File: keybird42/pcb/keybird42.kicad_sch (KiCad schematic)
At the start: 183 parts, among them SW1 SW_MX, SW10 SW_MX, SW11 SW_MX, SW12 SW_MX, SW13 SW_MX, SW14 SW_MX, SW15 SW_MX, SW16 SW_MX, SW17 SW_MX, SW18 SW_MX, SW19 SW_MX, SW2 SW_MX, SW20 SW_MX, SW21 SW_MX, SW22 SW_MX, SW23 SW_MX, SW24 SW_MX, SW25 SW_MX, SW26 SW_MX, SW27 SW_MX, SW28 SW_MX, SW29 SW_MX, SW3 SW_MX, SW30 SW_MX, SW31 SW_MX, SW32 SW_MX, SW33 SW_MX, SW34 SW_MX, SW35 SW_MX, SW36 SW_MX, SW37 SW_MX, SW38 SW_MX, SW39 SW_MX, SW4 SW_MX, SW40 SW_MX, SW41 SW_MX, SW42 SW_MX, SW43 SW_MX, SW44 SW_MX, SW45 SW_MX, SW46 SW_MX, SW47 SW_MX, SW48 SW_MX, SW49 SW_MX, SW5 SW_MX, SW50 SW_MX, SW51 SW_MX, SW52 SW_MX, SW53 SW_MX, SW54 SW_MX, SW55 SW_MX, SW56 SW_MX, SW57 SW_MX, SW58 SW_MX, SW59 SW_MX, SW6 SW_MX, SW60 SW_MX, SW61 SW_MX, SW62 SW_MX, SW63 SW_MX, SW64 SW_MX, SW65 SW_MX, SW66 SW_MX, SW67 SW_MX, SW68 SW_MX, SW69 SW_MX, SW7 SW_MX, SW70 SW_MX, SW71 SW_MX, SW72 SW_MX, SW73 SW_MX, SW74 SW_MX, SW75 SW_MX, SW76 SW_MX, SW77 SW_MX, SW78 SW_MX, SW79 SW_MX, SW8 SW_MX, SW80 SW_MX, SW81 SW_MX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

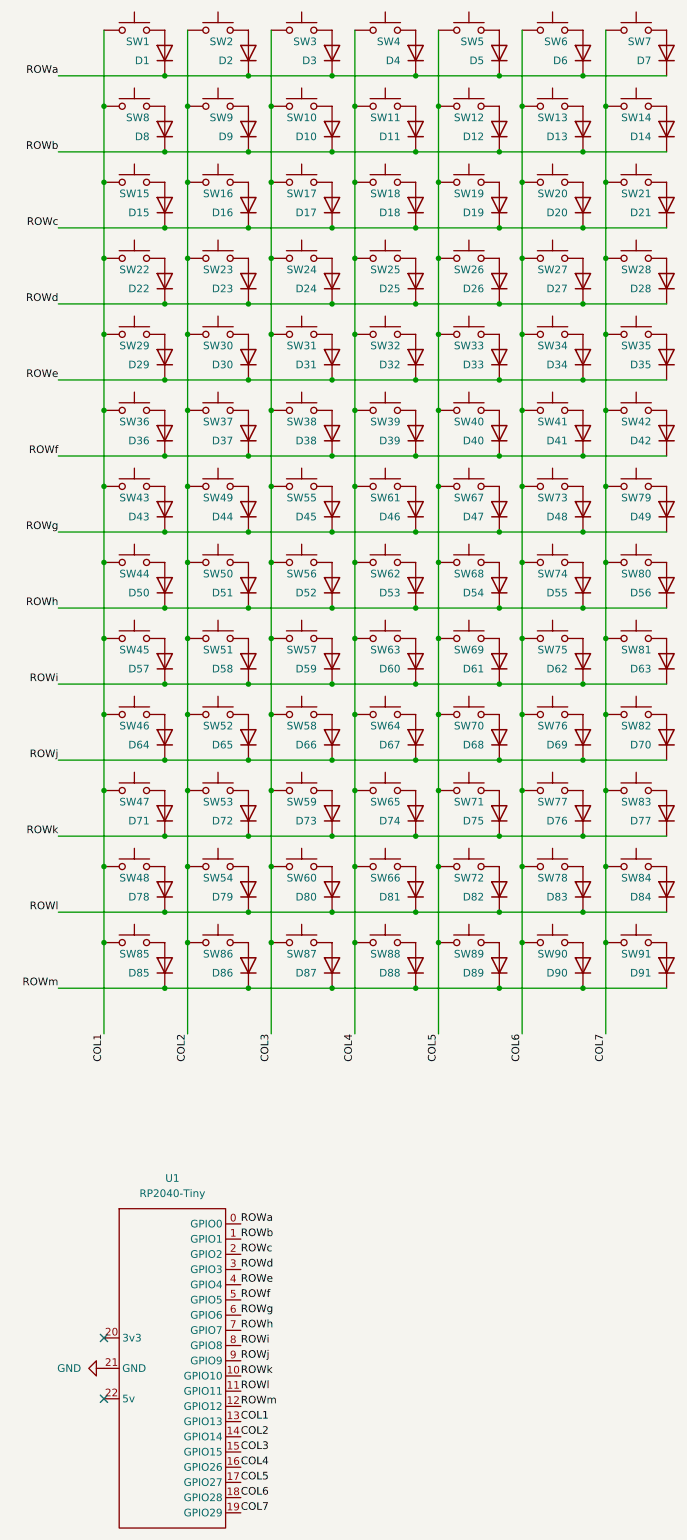
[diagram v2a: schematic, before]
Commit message: better row labels
two digits for row and sub-column

when these are used in switch and diode references, kicad is less
confused by pure digits
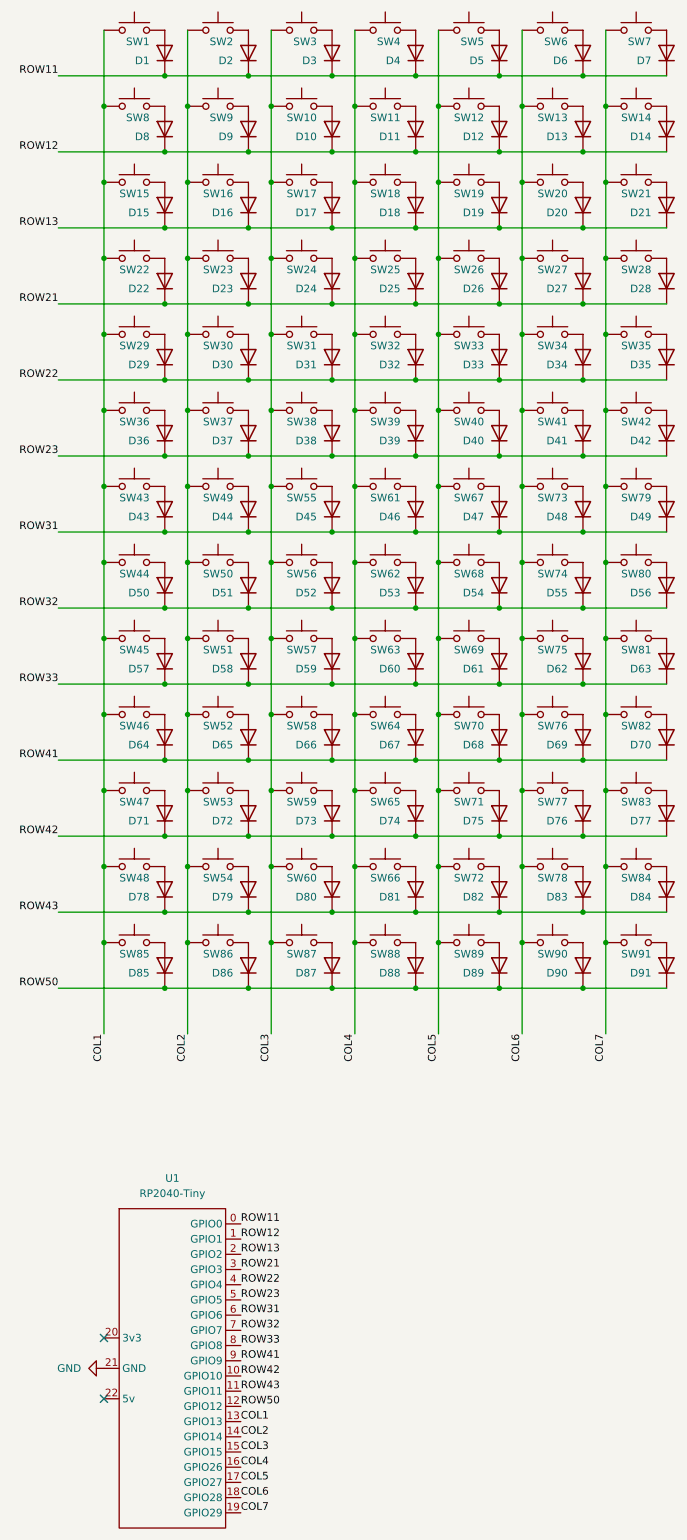
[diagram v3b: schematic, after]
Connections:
- net ROWa renamed ROW11
- net ROWb renamed ROW12
- net ROWc renamed ROW13
- net ROWd renamed ROW21
- net ROWe renamed ROW22
- net ROWf renamed ROW23
- net ROWg renamed ROW31
- net ROWh renamed ROW32
- net ROWi renamed ROW33
- net ROWj renamed ROW41
- net ROWk renamed ROW42
- net ROWl renamed ROW43
- net ROWm renamed ROW50
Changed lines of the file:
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@@
     (stroke (width 0) (type default))
   )
-  (label "ROWd" (at 55.88 224.79 0) (fields_autoplaced)
+  (label "ROW21" (at 55.88 224.79 0) (fields_autoplaced)
     (effects (font (size 1.27 1.27)) (justify left bottom))
   )
-  (label "ROWj" (at 25.4 139.7 180) (fields_autoplaced)
+  (label "ROW41" (at 25.4 139.7 180) (fields_autoplaced)
     (effects (font (size 1.27 1.27)) (justify right bottom))
   )
-  (label "ROWa" (at 25.4 25.4 180) (fields_autoplaced)
+  (label "ROW11" (at 25.4 25.4 180) (fields_autoplaced)
     (effects (font (size 1.27 1.27)) (justify right bottom))
   )
-  (label "ROWg" (at 25.4 101.6 180) (fields_autoplaced)
+  (label "ROW31" (at 25.4 101.6 180) (fields_autoplaced)
     (effects (font (size 1.27 1.27)) (justify right bottom))
   )
-  (label "ROWl" (at 55.88 245.11 0) (fields_autoplaced)
+  (label "ROW43" (at 55.88 245.11 0) (fields_autoplaced)
     (effects (font (size 1.27 1.27)) (justify left bottom))
   )
@@
     (effects (font (size 1.27 1.27)) (justify right bottom))
   )
-  (label "ROWc" (at 25.4 50.8 180) (fields_autoplaced)
+  (label "ROW13" (at 25.4 50.8 180) (fields_autoplaced)
     (effects (font (size 1.27 1.27)) (justify right bottom))
   )
-  (label "ROWb" (at 25.4 38.1 180) (fields_autoplaced)
+  (label "ROW12" (at 25.4 38.1 180) (fields_autoplaced)
     (effects (font (size 1.27 1.27)) (justify right bottom))
   )
-  (label "ROWi" (at 25.4 127 180) (fields_autoplaced)
+  (label "ROW33" (at 25.4 127 180) (fields_autoplaced)
     (effects (font (size 1.27 1.27)) (justify right bottom))
   )
-  (label "ROWe" (at 55.88 227.33 0) (fields_autoplaced)
+  (label "ROW22" (at 55.88 227.33 0) (fields_autoplaced)
     (effects (font (size 1.27 1.27)) (justify left bottom))
   )
-  (label "ROWd" (at 25.4 63.5 180) (fields_autoplaced)
+  (label "ROW21" (at 25.4 63.5 180) (fields_autoplaced)
     (effects (font (size 1.27 1.27)) (justify right bottom))
   )
-  (label "ROWf" (at 25.4 88.9 180) (fields_autoplaced)
+  (label "ROW23" (at 25.4 88.9 180) (fields_autoplaced)
     (effects (font (size 1.27 1.27)) (justify right bottom))
   )
-  (label "ROWm" (at 55.88 247.65 0) (fields_autoplaced)
+  (label "ROW50" (at 55.88 247.65 0) (fields_autoplaced)
     (effects (font (size 1.27 1.27)) (justify left bottom))
   )
-  (label "ROWh" (at 25.4 114.3 180) (fields_autoplaced)
+  (label "ROW32" (at 25.4 114.3 180) (fields_autoplaced)
     (effects (font (size 1.27 1.27)) (justify right bottom))
   )
@@
     (effects (font (size 1.27 1.27)) (justify left bottom))
   )
-  (label "ROWf" (at 55.88 229.87 0) (fields_autoplaced)
+  (label "ROW23" (at 55.88 229.87 0) (fields_autoplaced)
     (effects (font (size 1.27 1.27)) (justify left bottom))
   )
-  (label "ROWk" (at 25.4 152.4 180) (fields_autoplaced)
+  (label "ROW42" (at 25.4 152.4 180) (fields_autoplaced)
     (effects (font (size 1.27 1.27)) (justify right bottom))
   )
-  (label "ROWm" (at 25.4 177.8 180) (fields_autoplaced)
+  (label "ROW50" (at 25.4 177.8 180) (fields_autoplaced)
     (effects (font (size 1.27 1.27)) (justify right bottom))
   )
-  (label "ROWh" (at 55.88 234.95 0) (fields_autoplaced)
+  (label "ROW32" (at 55.88 234.95 0) (fields_autoplaced)
     (effects (font (size 1.27 1.27)) (justify left bottom))
   )
-  (label "ROWl" (at 25.4 165.1 180) (fields_autoplaced)
+  (label "ROW43" (at 25.4 165.1 180) (fields_autoplaced)
     (effects (font (size 1.27 1.27)) (justify right bottom))
   )
@@
     (effects (font (size 1.27 1.27)) (justify left bottom))
   )
-  (label "ROWg" (at 55.88 232.41 0) (fields_autoplaced)
+  (label "ROW31" (at 55.88 232.41 0) (fields_autoplaced)
     (effects (font (size 1.27 1.27)) (justify left bottom))
   )
-  (label "ROWa" (at 55.88 217.17 0) (fields_autoplaced)
+  (label "ROW11" (at 55.88 217.17 0) (fields_autoplaced)
     (effects (font (size 1.27 1.27)) (justify left bottom))
   )
@@
     (effects (font (size 1.27 1.27)) (justify right bottom))
   )
-  (label "ROWe" (at 25.4 76.2 180) (fields_autoplaced)
+  (label "ROW22" (at 25.4 76.2 180) (fields_autoplaced)
     (effects (font (size 1.27 1.27)) (justify right bottom))
   )
@@
     (effects (font (size 1.27 1.27)) (justify left bottom))
   )
-  (label "ROWk" (at 55.88 242.57 0) (fields_autoplaced)
+  (label "ROW42" (at 55.88 242.57 0) (fields_autoplaced)
     (effects (font (size 1.27 1.27)) (justify left bottom))
   )
-  (label "ROWi" (at 55.88 237.49 0) (fields_autoplaced)
+  (label "ROW33" (at 55.88 237.49 0) (fields_autoplaced)
     (effects (font (size 1.27 1.27)) (justify left bottom))
   )
@@
     (effects (font (size 1.27 1.27)) (justify left bottom))
   )
-  (label "ROWj" (at 55.88 240.03 0) (fields_autoplaced)
+  (label "ROW41" (at 55.88 240.03 0) (fields_autoplaced)
     (effects (font (size 1.27 1.27)) (justify left bottom))
   )
-  (label "ROWc" (at 55.88 222.25 0) (fields_autoplaced)
+  (label "ROW13" (at 55.88 222.25 0) (fields_autoplaced)
     (effects (font (size 1.27 1.27)) (justify left bottom))
   )
@@
     (effects (font (size 1.27 1.27)) (justify right bottom))
   )
-  (label "ROWb" (at 55.88 219.71 0) (fields_autoplaced)
+  (label "ROW12" (at 55.88 219.71 0) (fields_autoplaced)
     (effects (font (size 1.27 1.27)) (justify left bottom))
   )

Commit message: use an evil perl script to fix the switch and diode references
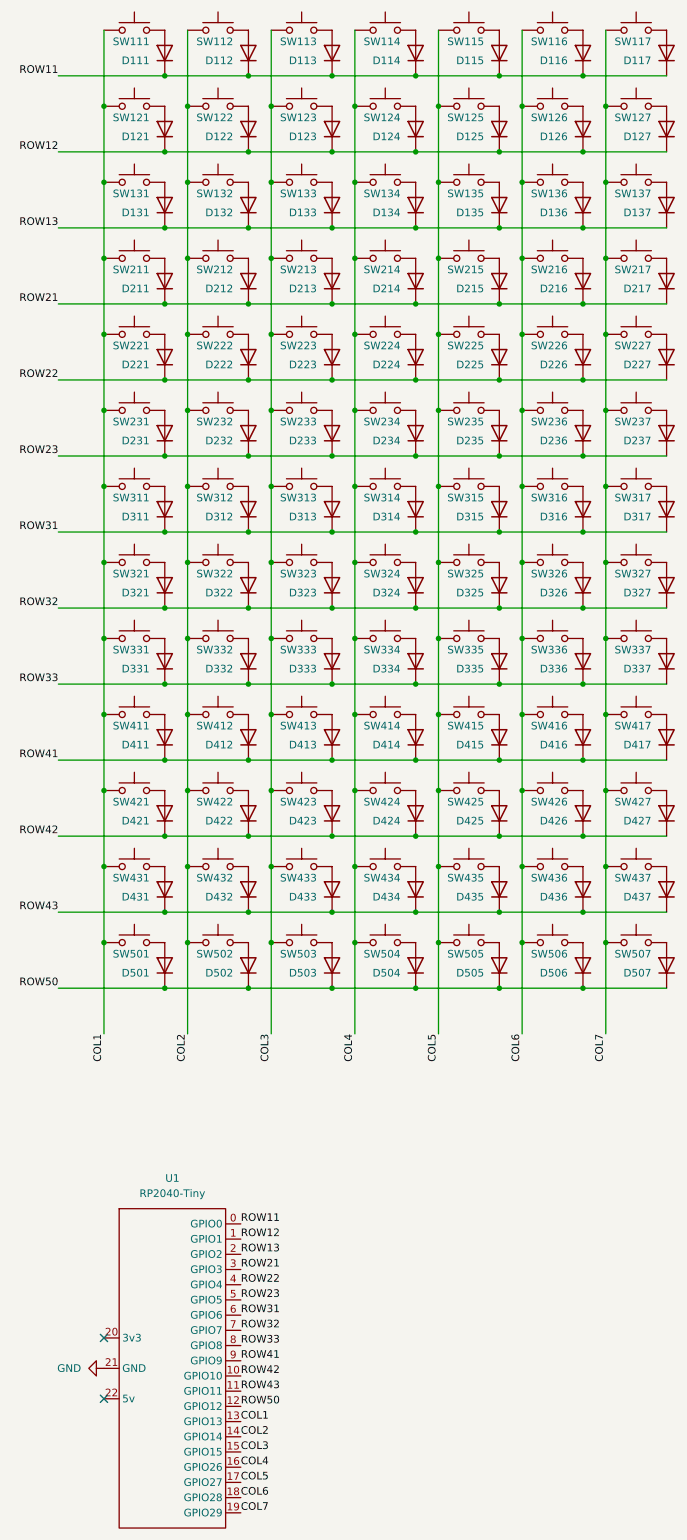
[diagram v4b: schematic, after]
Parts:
- renumbered D1 to D111, D2 to D112, D3 to D113, D4 to D114, D5 to D115, D6 to D116, D7 to D117, D8 to D121, D9 to D122, D10 to D123, D11 to D124, D12 to D125, D13 to D126, D14 to D127, D15 to D131, D16 to D132, D17 to D133, D18 to D134, D19 to D135, D20 to D136, D21 to D137, D22 to D211, D23 to D212, D24 to D213, D25 to D214, D26 to D215, D27 to D216, D28 to D217, D29 to D221, D30 to D222, D31 to D223, D32 to D224, D33 to D225, D34 to D226, D35 to D227, D36 to D231, D37 to D232, D38 to D233, D39 to D234, D40 to D235, D41 to D236, D42 to D237, D43 to D311, D44 to D312, D45 to D313, D46 to D314, D47 to D315, D48 to D316, D49 to D317, D50 to D321, D51 to D322, D52 to D323, D53 to D324, D54 to D325, D55 to D326, D56 to D327, D57 to D331, D58 to D332, D59 to D333, D60 to D334, D61 to D335, D62 to D336, D63 to D337, D64 to D411, D65 to D412, D66 to D413, D67 to D414, D68 to D415, D69 to D416, D70 to D417, D71 to D421, D72 to D422, D73 to D423, D74 to D424, D75 to D425, D76 to D426, D77 to D427, D78 to D431, D79 to D432, D80 to D433, D81 to D434, D82 to D435, D83 to D436, D84 to D437, D85 to D501, D86 to D502, D87 to D503, D88 to D504, D89 to D505, D90 to D506, D91 to D507, SW1 to SW111, SW2 to SW112, SW3 to SW113, SW4 to SW114, SW5 to SW115, SW6 to SW116, SW7 to SW117, SW8 to SW121, SW9 to SW122, SW10 to SW123, SW11 to SW124, SW12 to SW125, SW13 to SW126, SW14 to SW127, SW15 to SW131, SW16 to SW132, SW17 to SW133, SW18 to SW134, SW19 to SW135, SW20 to SW136, SW21 to SW137, SW22 to SW211, SW23 to SW212, SW24 to SW213, SW25 to SW214, SW26 to SW215, SW27 to SW216, SW28 to SW217, SW29 to SW221, SW30 to SW222, SW31 to SW223, SW32 to SW224, SW33 to SW225, SW34 to SW226, SW35 to SW227, SW36 to SW231, SW37 to SW232, SW38 to SW233, SW39 to SW234, SW40 to SW235, SW41 to SW236, SW42 to SW237, SW43 to SW311, SW49 to SW312, SW55 to SW313, SW61 to SW314, SW67 to SW315, SW73 to SW316, SW79 to SW317, SW44 to SW321, SW50 to SW322, SW56 to SW323, SW62 to SW324, SW68 to SW325, SW74 to SW326, SW80 to SW327, SW45 to SW331, SW51 to SW332, SW57 to SW333, SW63 to SW334, SW69 to SW335, SW75 to SW336, SW81 to SW337, SW46 to SW411, SW52 to SW412, SW58 to SW413, SW64 to SW414, SW70 to SW415, SW76 to SW416, SW82 to SW417, SW47 to SW421, SW53 to SW422, SW59 to SW423, SW65 to SW424, SW71 to SW425, SW77 to SW426, SW83 to SW427, SW48 to SW431, SW54 to SW432, SW60 to SW433, SW66 to SW434, SW72 to SW435, SW78 to SW436, SW84 to SW437, SW85 to SW501, SW86 to SW502, SW87 to SW503, SW88 to SW504, SW89 to SW505, SW90 to SW506, SW91 to SW507

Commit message: start placing switches on the pcb
first two rows roughly in place, not properly aligned yet
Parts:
- removed D224: 1N4148W, Diode_SMD:D_SOD-123, symbol keybird42:1N4148W
- removed SW224: SW_MX, PCM_Switch_Keyboard_Hotswap_Kailh:SW_Hotswap_Kailh_MX, symbol keybird42:SW_MX
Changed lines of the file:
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@@
   (junction (at 102.87 157.48) (diameter 0) (color 0 0 0 0)
   )
-  (junction (at 74.93 68.58) (diameter 0) (color 0 0 0 0)
-  )
   (junction (at 43.18 152.4) (diameter 0) (color 0 0 0 0)
   )
@@
   (junction (at 46.99 30.48) (diameter 0) (color 0 0 0 0)
   )
-  (junction (at 85.09 76.2) (diameter 0) (color 0 0 0 0)
-  )
   (junction (at 116.84 30.48) (diameter 0) (color 0 0 0 0)
   )
@@
     (stroke (width 0) (type default))
   )
-  (wire (pts (xy 74.93 55.88) (xy 74.93 68.58))
+  (wire (pts (xy 74.93 55.88) (xy 74.93 81.28))
     (stroke (width 0) (type default))
   )
@@
     (stroke (width 0) (type default))
   )
-  (wire (pts (xy 85.09 76.2) (xy 99.06 76.2))
-    (stroke (width 0) (type default))
-  )
   (wire (pts (xy 116.84 170.18) (xy 116.84 185.42))
     (stroke (width 0) (type default))
@@
     (stroke (width 0) (type default))
   )
-  (wire (pts (xy 74.93 68.58) (xy 74.93 81.28))
-    (stroke (width 0) (type default))
-  )
   (wire (pts (xy 33.02 119.38) (xy 33.02 132.08))
     (stroke (width 0) (type default))
@@
     (stroke (width 0) (type default))
   )
-  (wire (pts (xy 71.12 76.2) (xy 85.09 76.2))
+  (wire (pts (xy 71.12 76.2) (xy 99.06 76.2))
     (stroke (width 0) (type default))
   )
@@
     )
   )
-  (symbol (lib_id "keybird42:SW_MX") (at 80.01 68.58 0) (unit 1)
-    (in_bom yes) (on_board yes) (dnp no)
-    (property "Reference" "SW224" (at 82.55 70.485 0) (do_not_autoplace)
-      (effects (font (size 1.27 1.27)) (justify right))
-    )
-    (property "Value" "SW_MX" (at 80.01 63.5 0)
-      (effects (font (size 1.27 1.27)) hide)
-    )
-    (property "Footprint" "PCM_Switch_Keyboard_Hotswap_Kailh:SW_Hotswap_Kailh_MX" (at 80.01 60.96 0)
-      (effects (font (size 1.27 1.27)) hide)
-    )
-    (property "Datasheet" "~" (at 80.01 63.5 0)
-      (effects (font (size 1.27 1.27)) hide)
-    )
-    (pin "2")
-    (pin "1")
-    (instances
-      (project "keybird42"
-        (path "/c6489b6f-cd36-4929-9d41-a438ed9c3e88"
-          (reference "SW224") (unit 1)
-        )
-      )
-    )
-  )
   (symbol (lib_id "keybird42:SW_MX") (at 80.01 106.68 0) (unit 1)
     (in_bom yes) (on_board yes) (dnp no)
@@
         )
       )
-    )
-  )
-  (symbol (lib_id "keybird42:1N4148W") (at 85.09 72.39 0) (unit 1)
-    (in_bom yes) (on_board yes) (dnp no) (fields_autoplaced)
-    (property "Reference" "D224" (at 82.55 73.66 0) (do_not_autoplace)
-      (effects (font (size 1.27 1.27)) (justify right))
-    )
-    (property "Value" "1N4148W" (at 85.09 80.01 0)
-      (effects (font (size 1.27 1.27)) hide)
-    )
-    (property "Footprint" "Diode_SMD:D_SOD-123" (at 85.09 82.55 0)
-      (effects (font (size 1.27 1.27)) hide)
-    )
-    (property "Datasheet" "https://www.vishay.com/docs/85748/1n4148w.pdf" (at 85.09 85.09 0)
-      (effects (font (size 1.27 1.27)) hide)
-    )
-    (property "Sim.Device" "D" (at 85.09 77.47 0)
-      (effects (font (size 1.27 1.27)) hide)
-    )
-    (property "Sim.Pins" "1=K 2=A" (at 88.9 72.39 90)
-      (effects (font (size 1.27 1.27)) hide)
-    )
-    (pin "1")
-    (pin "2")
-    (instances
-      (project "keybird42"
-        (path "/c6489b6f-cd36-4929-9d41-a438ed9c3e88"
-          (reference "D224") (unit 1)
-        )
-      )

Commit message: row 3, two more gaps
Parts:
- removed D313, D326: 1N4148W, Diode_SMD:D_SOD-123, symbol keybird42:1N4148W
- removed SW313, SW326: SW_MX, PCM_Switch_Keyboard_Hotswap_Kailh:SW_Hotswap_Kailh_MX, symbol keybird42:SW_MX
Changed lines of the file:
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@@
   (junction (at 57.15 152.4) (diameter 0) (color 0 0 0 0)
   )
-  (junction (at 71.12 101.6) (diameter 0) (color 0 0 0 0)
-  )
   (junction (at 74.93 157.48) (diameter 0) (color 0 0 0 0)
   )
@@
   (junction (at 99.06 177.8) (diameter 0) (color 0 0 0 0)
   )
-  (junction (at 113.03 114.3) (diameter 0) (color 0 0 0 0)
-  )
   (junction (at 71.12 88.9) (diameter 0) (color 0 0 0 0)
   )
@@
   (junction (at 71.12 50.8) (diameter 0) (color 0 0 0 0)
   )
-  (junction (at 102.87 106.68) (diameter 0) (color 0 0 0 0)
-  )
   (junction (at 43.18 127) (diameter 0) (color 0 0 0 0)
   )
@@
   (junction (at 43.18 165.1) (diameter 0) (color 0 0 0 0)
   )
-  (junction (at 60.96 93.98) (diameter 0) (color 0 0 0 0)
-  )
   (junction (at 57.15 114.3) (diameter 0) (color 0 0 0 0)
   )
@@
   (no_connect (at 33.02 246.38))
   (no_connect (at 33.02 236.22))
-  (wire (pts (xy 113.03 114.3) (xy 127 114.3))
+  (wire (pts (xy 99.06 114.3) (xy 127 114.3))
     (stroke (width 0) (type default))
   )
@@
     (stroke (width 0) (type default))
   )
-  (wire (pts (xy 60.96 81.28) (xy 60.96 93.98))
+  (wire (pts (xy 60.96 81.28) (xy 60.96 106.68))
     (stroke (width 0) (type default))
   )
@@
     (stroke (width 0) (type default))
   )
-  (wire (pts (xy 102.87 106.68) (xy 102.87 119.38))
-    (stroke (width 0) (type default))
-  )
   (wire (pts (xy 116.84 170.18) (xy 116.84 185.42))
     (stroke (width 0) (type default))
@@
     (stroke (width 0) (type default))
   )
-  (wire (pts (xy 99.06 114.3) (xy 113.03 114.3))
-    (stroke (width 0) (type default))
-  )
   (wire (pts (xy 57.15 152.4) (xy 71.12 152.4))
     (stroke (width 0) (type default))
@@
     (stroke (width 0) (type default))
   )
-  (wire (pts (xy 71.12 101.6) (xy 85.09 101.6))
-    (stroke (width 0) (type default))
-  )
   (wire (pts (xy 74.93 81.28) (xy 74.93 93.98))
     (stroke (width 0) (type default))
@@
     (stroke (width 0) (type default))
   )
-  (wire (pts (xy 57.15 101.6) (xy 71.12 101.6))
-    (stroke (width 0) (type default))
-  )
-  (wire (pts (xy 60.96 93.98) (xy 60.96 106.68))
+  (wire (pts (xy 57.15 101.6) (xy 85.09 101.6))
     (stroke (width 0) (type default))
   )
@@
     (stroke (width 0) (type default))
   )
-  (wire (pts (xy 102.87 93.98) (xy 102.87 106.68))
+  (wire (pts (xy 102.87 93.98) (xy 102.87 119.38))
     (stroke (width 0) (type default))
   )
@@
     )
   )
-  (symbol (lib_id "keybird42:1N4148W") (at 113.03 110.49 0) (unit 1)
-    (in_bom yes) (on_board yes) (dnp no) (fields_autoplaced)
-    (property "Reference" "D326" (at 110.49 111.76 0) (do_not_autoplace)
-      (effects (font (size 1.27 1.27)) (justify right))
-    )
-    (property "Value" "1N4148W" (at 113.03 118.11 0)
-      (effects (font (size 1.27 1.27)) hide)
-    )
-    (property "Footprint" "Diode_SMD:D_SOD-123" (at 113.03 120.65 0)
-      (effects (font (size 1.27 1.27)) hide)
-    )
-    (property "Datasheet" "https://www.vishay.com/docs/85748/1n4148w.pdf" (at 113.03 123.19 0)
-      (effects (font (size 1.27 1.27)) hide)
-    )
-    (property "Sim.Device" "D" (at 113.03 115.57 0)
-      (effects (font (size 1.27 1.27)) hide)
-    )
-    (property "Sim.Pins" "1=K 2=A" (at 116.84 110.49 90)
-      (effects (font (size 1.27 1.27)) hide)
-    )
-    (pin "1")
-    (pin "2")
-    (instances
-      (project "keybird42"
-        (path "/c6489b6f-cd36-4929-9d41-a438ed9c3e88"
-          (reference "D326") (unit 1)
-        )
-      )
-    )
-  )
   (symbol (lib_id "keybird42:1N4148W") (at 71.12 135.89 0) (unit 1)
     (in_bom yes) (on_board yes) (dnp no) (fields_autoplaced)
@@
     )
   )
-  (symbol (lib_id "keybird42:SW_MX") (at 107.95 106.68 0) (unit 1)
-    (in_bom yes) (on_board yes) (dnp no)
-    (property "Reference" "SW326" (at 110.49 108.585 0) (do_not_autoplace)
-      (effects (font (size 1.27 1.27)) (justify right))
-    )
-    (property "Value" "SW_MX" (at 107.95 101.6 0)
-      (effects (font (size 1.27 1.27)) hide)
-    )
-    (property "Footprint" "PCM_Switch_Keyboard_Hotswap_Kailh:SW_Hotswap_Kailh_MX" (at 107.95 99.06 0)
-      (effects (font (size 1.27 1.27)) hide)
-    )
-    (property "Datasheet" "~" (at 107.95 101.6 0)
-      (effects (font (size 1.27 1.27)) hide)
-    )
-    (pin "2")
-    (pin "1")
-    (instances
-      (project "keybird42"
-        (path "/c6489b6f-cd36-4929-9d41-a438ed9c3e88"
-          (reference "SW326") (unit 1)
-        )
-      )
-    )
-  )
   (symbol (lib_id "keybird42:1N4148W") (at 85.09 85.09 0) (unit 1)
     (in_bom yes) (on_board yes) (dnp no) (fields_autoplaced)
@@
     )
   )
-  (symbol (lib_id "keybird42:1N4148W") (at 71.12 97.79 0) (unit 1)
-    (in_bom yes) (on_board yes) (dnp no) (fields_autoplaced)
-    (property "Reference" "D313" (at 68.58 99.06 0) (do_not_autoplace)
-      (effects (font (size 1.27 1.27)) (justify right))
-    )
-    (property "Value" "1N4148W" (at 71.12 105.41 0)
-      (effects (font (size 1.27 1.27)) hide)
-    )
-    (property "Footprint" "Diode_SMD:D_SOD-123" (at 71.12 107.95 0)
-      (effects (font (size 1.27 1.27)) hide)
-    )
-    (property "Datasheet" "https://www.vishay.com/docs/85748/1n4148w.pdf" (at 71.12 110.49 0)
-      (effects (font (size 1.27 1.27)) hide)
-    )
-    (property "Sim.Device" "D" (at 71.12 102.87 0)
-      (effects (font (size 1.27 1.27)) hide)
-    )
-    (property "Sim.Pins" "1=K 2=A" (at 74.93 97.79 90)
-      (effects (font (size 1.27 1.27)) hide)
-    )
-    (pin "1")
-    (pin "2")
-    (instances
-      (project "keybird42"
-        (path "/c6489b6f-cd36-4929-9d41-a438ed9c3e88"
-          (reference "D313") (unit 1)
-        )
-      )
-    )
-  )
   (symbol (lib_id "keybird42:SW_MX") (at 121.92 144.78 0) (unit 1)
     (in_bom yes) (on_board yes) (dnp no)
@@
         )
       )
-    )
-  )
-  (symbol (lib_id "keybird42:SW_MX") (at 66.04 93.98 0) (unit 1)
-    (in_bom yes) (on_board yes) (dnp no)
-    (property "Reference" "SW313" (at 68.58 95.885 0) (do_not_autoplace)
-      (effects (font (size 1.27 1.27)) (justify right))
-    )
-    (property "Value" "SW_MX" (at 66.04 88.9 0)
-      (effects (font (size 1.27 1.27)) hide)
-    )
-    (property "Footprint" "PCM_Switch_Keyboard_Hotswap_Kailh:SW_Hotswap_Kailh_MX" (at 66.04 86.36 0)
-      (effects (font (size 1.27 1.27)) hide)
-    )
-    (property "Datasheet" "~" (at 66.04 88.9 0)
-      (effects (font (size 1.27 1.27)) hide)
-    )
-    (pin "2")
-    (pin "1")
-    (instances
-      (project "keybird42"
-        (path "/c6489b6f-cd36-4929-9d41-a438ed9c3e88"
-          (reference "SW313") (unit 1)
-        )
-      )
